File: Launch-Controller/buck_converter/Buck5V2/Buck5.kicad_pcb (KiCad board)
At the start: 4 copper layers, 30.5 x 45.8 mm, 12 parts, among them J1 Conn_01x10_Socket, U1 LM2596S-5

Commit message: LC cosmetic updates
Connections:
- Cin1 pad 2: /GND -> GND
- Cout1 pad 2: /GND -> GND
- D1 pad 1: /GND -> GND
- D2 pad 2: /GND -> GND
- D3 pad 1: /GND -> GND
- H1 pad 1: unconnected-(H1-Pad1) -> GND
- H2 pad 1: unconnected-(H2-Pad1) -> GND
- J1 pad 1: /GND -> GND
- J1 pad 2: /GND -> GND
- J1 pad 3: /GND -> GND
- J1 pad 4: /GND -> GND
- J1 pad 5: /GND -> GND
- J1 pad 6: /GND -> GND
- J1 pad 7: /GND -> GND
- J1 pad 8: /GND -> GND
- U1 pad 3: /GND -> GND
- U1 pad 5: /GND -> GND
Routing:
- added copper zone on F.Cu, net GND
- removed copper zone on F.Cu, net /GND

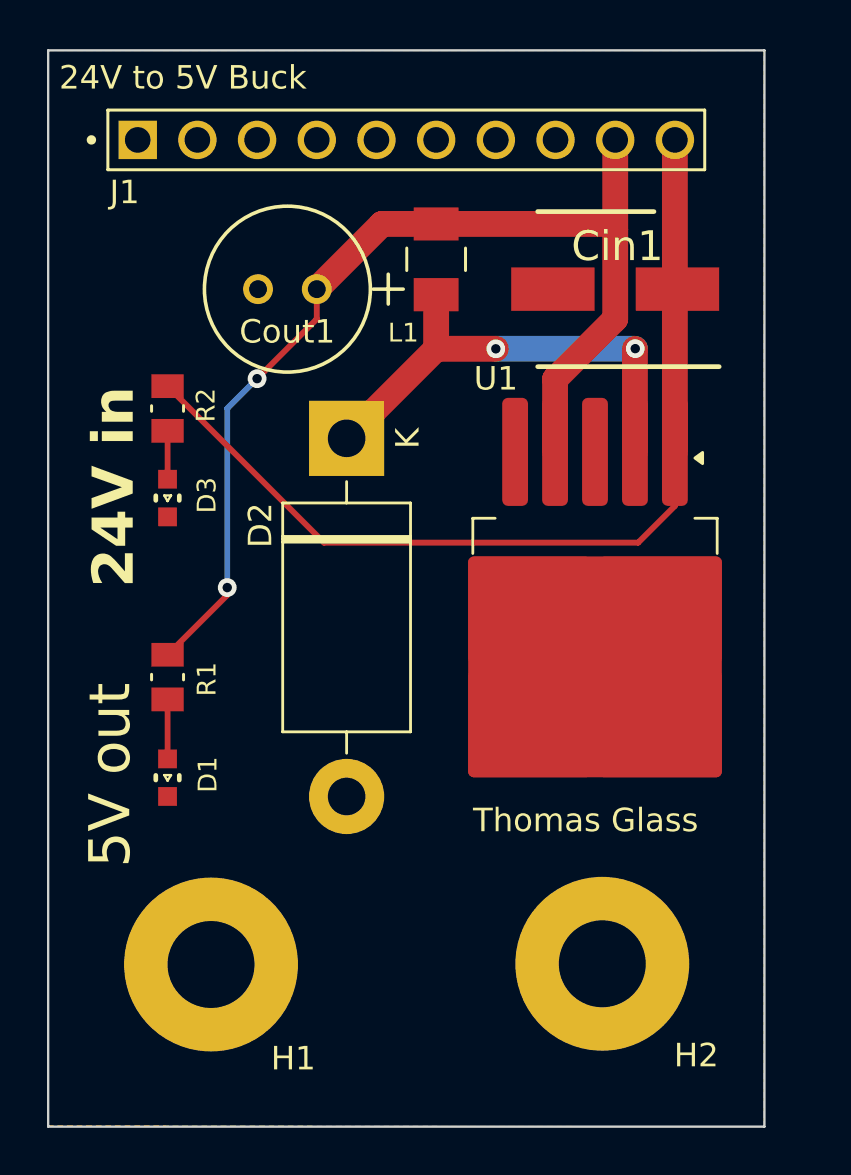
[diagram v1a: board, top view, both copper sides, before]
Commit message: buck converter v2 changes
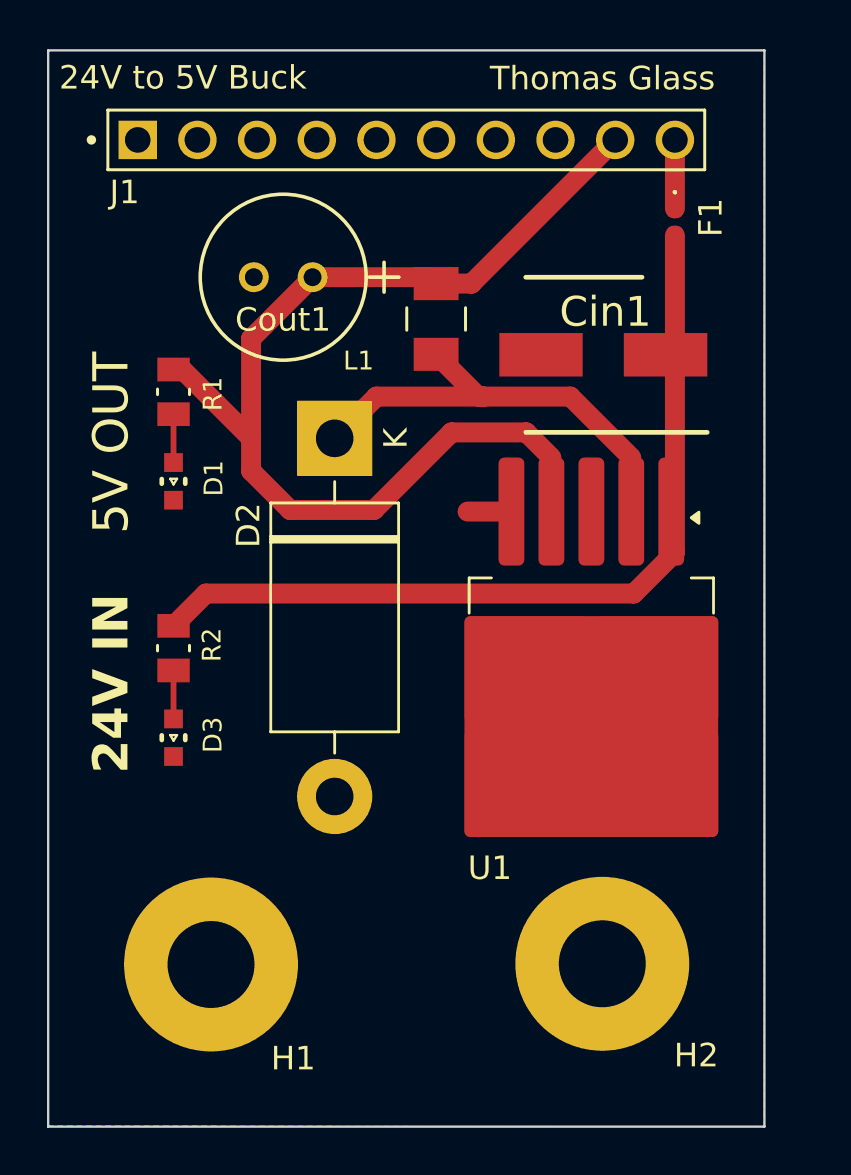
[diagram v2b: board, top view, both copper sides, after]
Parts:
- added F1: Fuse, Diode_SMD:D_0402_1005Metric_Pad0.77x0.64mm_HandSolder, F.Cu at (123.2, 77.2)
- moved D1 12.6 mm to (101.9, 88.2)
- moved R1 12.1 mm to (101.9, 84.4)
- moved D3 10.2 mm to (101.9, 99.1)
- moved R2 10.2 mm to (101.9, 95.3)
- moved Cin1 2.84 mm to (120.1, 82.8)
- moved U1 2.54 mm to (119.6, 97.1)
- moved L1 2.54 mm to (113.0, 81.3)
- moved Cout1 0.54 mm to (107.8, 79.5)
- moved D2 0.51 mm to (108.7, 86.4)
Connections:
- Cin1 pad 1: /+24V -> Net-(U1-VIN)
- R2 pad 1: /+24V -> Net-(U1-VIN)
- U1 pad 1: /+24V -> Net-(U1-VIN)
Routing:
- net /+24V: track 40.6 -> 2.92 mm
- net Net-(U1-VIN): track 0.00 -> 36.8 mm
- net GND: track 0.00 -> 1.87 mm
- net Net-(D2-K): track 20.6 -> 19.5 mm, vias 2 -> 0
- net /+5V: track 46.5 -> 46.9 mm, vias 2 -> 0
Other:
- board text added: "24V IN"
- board text added: "5V OUT"
- board text removed: "24V in"
- board text removed: "5V out"

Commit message: redone buck converter
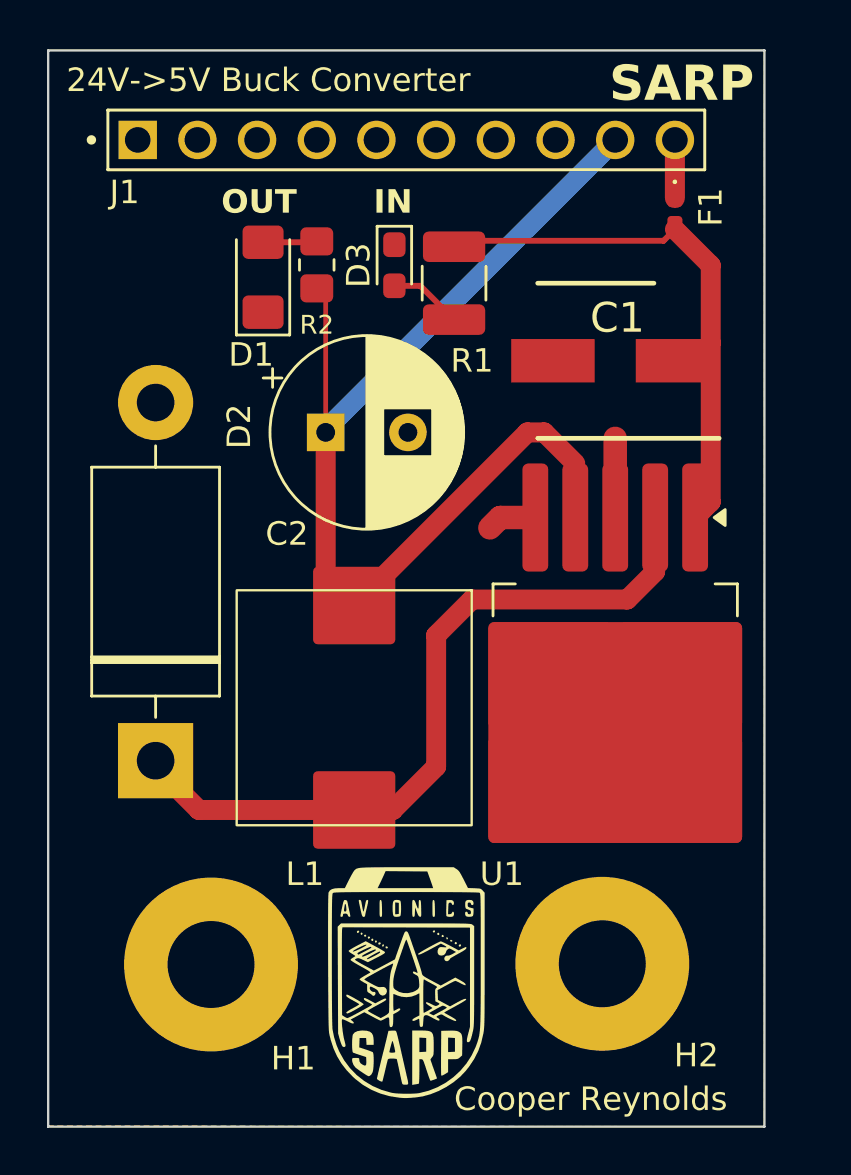
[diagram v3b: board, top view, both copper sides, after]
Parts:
- removed Cin1: 680u, KiCad:CAPAE660X800N
- removed Cout1: 220u, footprints:CAP_YX_6P3X11_RUB
- added C1: 680uF, Library:CAPAE660X800N, F.Cu at (120.7, 83.1)
- added C2: 330uF, Capacitor_THT:CP_Radial_D8.0mm_P3.50mm, F.Cu at (108.3, 86.1)
- added G***: LOGO, kicad_import:7mm shield avionics, F.Cu at (111.8, 109.5)
- D1: value 150060VS75000 -> red; footprint WL-SMCW_0603:WL-SMCW_0603 -> LED_SMD:LED_1206_3216Metric_Pad1.42x1.75mm_HandSolder
- D3: value 150060RS75000 -> green; footprint WL-SMCW_0603:WL-SMCW_0603 -> LED_SMD:LED_0603_1608Metric_Pad1.05x0.95mm_HandSolder
- J1: footprint 10pin Socket:PRECI-DIP_310-87-110-41-001101 -> Library:PRECI-DIP_310-87-110-41-001101
- L1: value 33u -> 47uH; footprint NLCV32T_330K_EF:INDM3225X240N -> Library:output inductor
- R1: value 1.1k -> 1100Ω; footprint RMCF0805JT1K10:RESC2012X65N -> Resistor_SMD:R_1210_3225Metric_Pad1.30x2.65mm_HandSolder
- R2: value 1.1k -> 150Ω; footprint RMCF0805JT1K10:RESC2012X65N -> Resistor_SMD:R_0805_2012Metric_Pad1.20x1.40mm_HandSolder
- moved D3 22.2 mm to (111.3, 79.0), turned to -90 degrees
- moved R2 17.4 mm to (108.0, 79.0), turned to 90 degrees
- moved L1 15.8 mm to (98.9, 88.4), turned to -90 degrees
- moved D2 15.7 mm to (101.1, 100.1), turned to 90 degrees
- moved R1 12.8 mm to (113.8, 79.8)
- moved D1 9.49 mm to (105.7, 79.5)
- moved U1 1.05 mm to (120.7, 97.4)
- moved F1 0.44 mm to (123.2, 76.7)
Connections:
- R1 pad 1: /+5V -> Net-(U1-VIN)
- R1 pad 2: Net-(D1-Pad2) -> Net-(D3-Pad2)
- R2 pad 1: Net-(U1-VIN) -> /+5V
- R2 pad 2: Net-(D3-Pad2) -> Net-(D1-Pad2)
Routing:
- net Net-(D2-K): track 19.5 -> 33.8 mm
- net Net-(U1-VIN): track 36.8 -> 23.0 mm
- net GND: track 1.87 -> 5.49 mm
- net Net-(D3-Pad2): track 2.06 -> 3.14 mm
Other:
- board text added: "24V->5V Buck Converter"
- board text added: "Cooper Reynolds"
- board text added: "IN"
- board text added: "OUT"
- board text added: "SARP"
- board text removed: "24V IN"
- board text removed: "24V to 5V Buck"
- board text removed: "5V OUT"
- board text removed: "Thomas Glass"
